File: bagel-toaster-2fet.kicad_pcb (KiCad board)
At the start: 2 copper layers, 144.4 x 105.1 mm, 121 parts, among them J1 bs, J10 9v, J11 9v, J12 9v, J13 9v, J14 o1b, J15 gnd, J16 gnd, J17 gnd, J18 gnd, J19 i2b, J2 do_snd, J20 o2b, J21 i2, J22 i2s, J23 gnd, J24 o2, J25 9v, J26 o2s, J27 i1, J28 i1s, J29 gnd, J3 out, J30 o1, J31 9v, J32 o1s, J4 in, J5 do_rtn, J6 i1b, J7 bs, J8 gnd, J9 9v, Q1 J113, Q2 J201, SW1 3pdt, SW2 Alpha_3PDT, SW3 Alpha_3PDT, SW4 Alpha_3PDT, U1 TL074, U2 4069

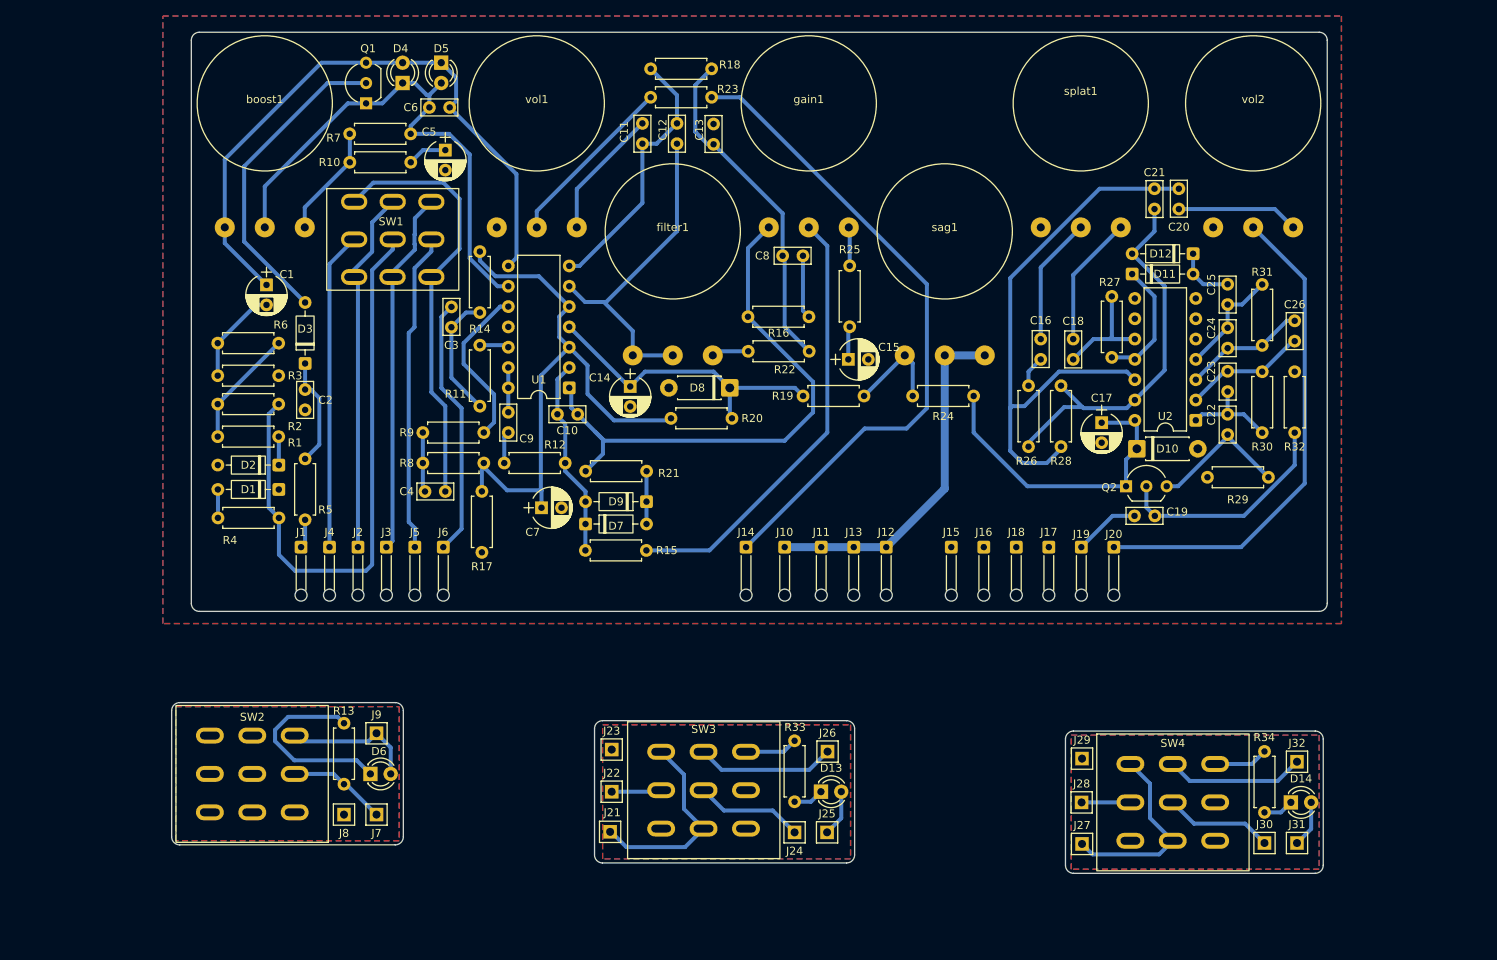
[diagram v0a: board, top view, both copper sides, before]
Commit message: one sided and smaller
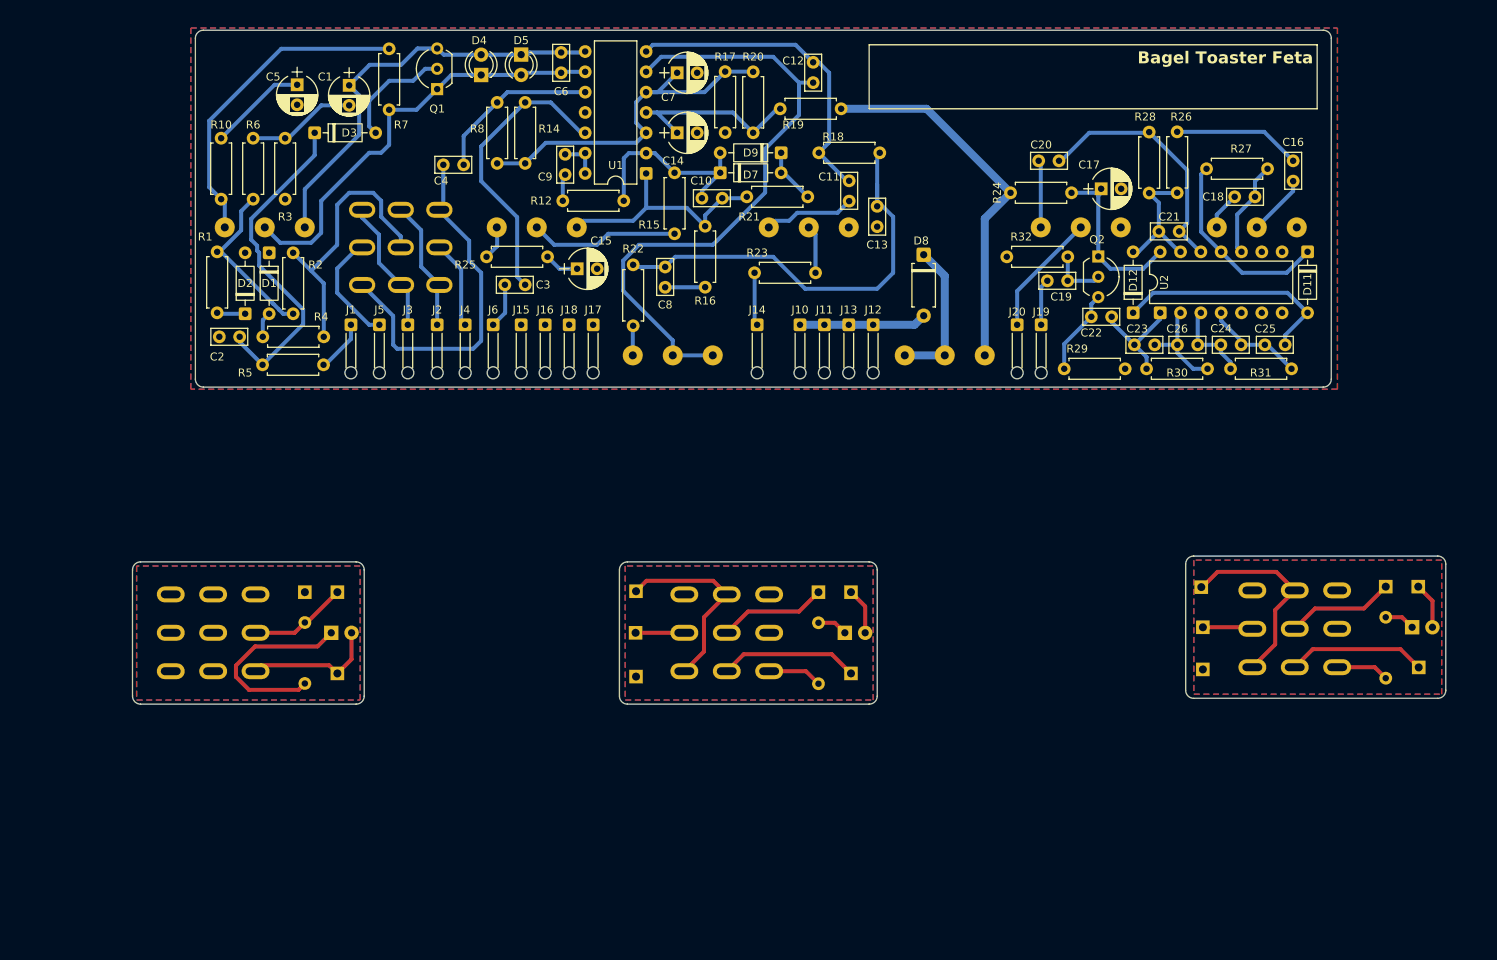
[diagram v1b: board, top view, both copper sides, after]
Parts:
- removed D10: 1N4001, Diode_THT:D_DO-41_SOD81_P7.62mm_Horizontal
- removed R11, R9: 100, 1_trevortjes_lib:R_1x4
- D13, D14, D6, J21, J22, J23, J24, J25, J26, J27, J28, J29, J30, J31, J32, J7, J8, J9, R13, R33, R34, SW1, SW2, SW3, SW4, boost1, filter1, gain1, sag1, splat1, vol1, vol2: moved to B.Cu
- D8: value 1N4001 -> D_Schottky; footprint Diode_THT:D_DO-41_SOD81_P7.62mm_Horizontal -> Diode_THT:D_A-405_P7.62mm_Horizontal
- moved J24 80.0 mm to (214.1, 96.7)
- moved J25 80.0 mm to (218.1, 96.7)
- moved J21 80.0 mm to (191.0, 96.8), turned to 90 degrees
- moved D13 76.7 mm to (217.4, 101.8)
- moved J22 76.7 mm to (191.2, 101.8)
- moved SW3 76.6 mm to (202.7, 102.0)
- moved J26 74.6 mm to (218.2, 106.8)
- moved J23 74.6 mm to (191.2, 107.1)
- moved R33 74.3 mm to (214.1, 108.2), turned to 90 degrees
- moved J27 64.1 mm to (120.4, 97.3)
- moved J30 64.0 mm to (143.2, 97.4)
- moved J31 64.0 mm to (147.2, 97.4)
- moved J17 63.4 mm to (115.0, 64.0)
- moved J18 62.4 mm to (112.0, 64.0)
- moved J16 61.5 mm to (109.0, 64.0)
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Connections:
- C3 pad 2: Net-(C3-Pad2) -> Net-(U1D-+)
- C4 pad 2: Net-(C4-Pad2) -> Net-(U1C-+)
- D8 pad 1: /v2 -> Net-(D8-K)
- D8 pad 2: GND -> /9v
- R14 pad 2: Net-(C3-Pad2) -> Net-(U1D-+)
- R26 pad 1: Net-(C16-Pad2) -> Net-(C16-Pad1)
- R8 pad 1: Net-(C4-Pad2) -> Net-(U1C-+)
- sag1 pad 2: /9v -> Net-(D8-K)
- sag1 pad 3: /9v -> Net-(D8-K)
- splat1 pad 2: Net-(C16-Pad1) -> Net-(C16-Pad2)
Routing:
- net Net-(J14-Pin_1): track 81.9 -> 6.63 mm
- net Net-(J20-Pin_1): track 61.8 -> 15.5 mm
- net Net-(C20-Pad1): track 73.2 -> 31.3 mm
- net /gainOut: track 69.7 -> 29.8 mm
- net /b_rtn: track 74.4 -> 35.1 mm
- net Net-(U1B--): track 42.1 -> 79.2 mm
- net Net-(R15-Pad2): track 55.3 -> 18.7 mm
- net Net-(R19-Pad1): track 12.7 -> 47.2 mm
- net Net-(U1D-+): track 3.66 -> 36.4 mm
- net Net-(D12-A): track 48.1 -> 16.8 mm
- net /d_snd: track 45.4 -> 16.5 mm
- net /fx_out: track 45.5 -> 16.7 mm
- net /9v: track 44.7 -> 15.9 mm
- net /fx_in: track 39.7 -> 11.0 mm
- net /vref: track 74.1 -> 45.7 mm
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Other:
- board size 144.4 x 105.1 mm -> 164.2 x 84.2 mm
- board text added: "Bagel Toaster Feta"

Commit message: tidier
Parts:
- moved J17 50.2 mm to (156.0, 35.0), turned to 180 degrees
- moved J12 30.5 mm to (159.5, 35.0), turned to 180 degrees
- moved C8 18.5 mm to (142.5, 58.0), turned to 180 degrees
- moved C3 13.6 mm to (102.5, 45.5)
- moved C13 12.8 mm to (151.3, 39.0), turned to 0 degrees
- moved R22 9.92 mm to (127.5, 63.0), turned to 180 degrees
- moved C20 8.38 mm to (181.2, 41.0)
- moved D8 8.21 mm to (159.0, 63.0), turned to 90 degrees
- moved R23 5.49 mm to (136.5, 62.8), turned to 90 degrees
- moved C4 4.91 mm to (100.5, 41.5), turned to 90 degrees
- moved J14 4.50 mm to (140.0, 64.0)
- moved C10 4.33 mm to (131.5, 45.0), turned to -90 degrees
- moved J6 3.50 mm to (106.0, 64.0)
- moved R12 3.50 mm to (115.3, 48.5)
- moved R14 3.36 mm to (103.7, 42.0), turned to 0 degrees
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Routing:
- net Net-(U1D-+): track 36.4 -> 11.3 mm
- net /9v: track 15.9 -> 40.1 mm
- net /vref: track 45.7 -> 65.1 mm
- net Net-(J6-Pin_1): track 5.64 -> 20.0 mm
- net Net-(C13-Pad2): track 54.3 -> 42.2 mm
- net Net-(R19-Pad1): track 47.2 -> 59.1 mm
- net Net-(C20-Pad1): track 31.3 -> 20.4 mm
- net Net-(U1B--): track 79.2 -> 68.6 mm
- net Net-(D8-K): track 18.7 -> 9.84 mm
- net /gainOut: track 29.8 -> 35.8 mm
- net Net-(U1C-+): track 21.1 -> 15.2 mm
- net Net-(C20-Pad2): track 8.43 -> 14.0 mm
- net /b_snd: track 45.1 -> 49.6 mm
- net Net-(C8-Pad2): track 5.01 -> 9.37 mm
- net Net-(J14-Pin_1): track 6.63 -> 4.09 mm
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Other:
- board size 164.2 x 84.2 mm -> 164.2 x 83.9 mm

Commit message: smaller
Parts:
- J1: value bs -> bx; footprint Connector_Wire:SolderWire-0.1sqmm_1x01_D0.4mm_OD1mm_Relief -> Connector_Wire:SolderWire-0.5sqmm_1x01_D0.9mm_OD2.1mm
- J10, J11, J12, J13, J14, J15, J16, J17, J18, J19, J2, J20, J3, J4, J5, J6: footprint Connector_Wire:SolderWire-0.1sqmm_1x01_D0.4mm_OD1mm_Relief -> Connector_Wire:SolderWire-0.5sqmm_1x01_D0.9mm_OD2.1mm
- moved J18 47.6 mm to (162.5, 61.2)
- moved J16 46.3 mm to (158.2, 61.2)
- moved J15 45.1 mm to (154.0, 61.2)
- moved J12 34.6 mm to (137.0, 61.2), turned to 0 degrees
- moved J17 28.4 mm to (166.8, 61.2), turned to 0 degrees
- moved R33 26.4 mm to (198.3, 87.0)
- moved D13 26.4 mm to (201.6, 80.7)
- moved J24 26.4 mm to (198.3, 75.6)
- moved J25 26.4 mm to (202.4, 75.6)
- moved J21 26.4 mm to (175.2, 75.7)
- moved J22 26.4 mm to (175.4, 80.7)
- moved J23 26.4 mm to (175.4, 86.0)
- moved J26 26.4 mm to (202.4, 85.7)
- moved SW3 26.4 mm to (186.9, 80.9)
- moved C12 24.2 mm to (118.6, 30.0), turned to 0 degrees
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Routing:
- net Net-(U1B--): track 68.6 -> 16.5 mm
- net Net-(R19-Pad1): track 59.1 -> 12.6 mm
- net Net-(D3-K): track 43.5 -> 9.68 mm
- net Net-(R10-Pad2): track 40.4 -> 9.53 mm
- net Net-(C13-Pad2): track 42.2 -> 12.1 mm
- net Net-(D4-K): track 54.6 -> 25.8 mm
- net Net-(D12-A): track 15.1 -> 40.8 mm
- net Net-(D11-A): track 28.0 -> 5.88 mm
- net /b_snd: track 49.6 -> 28.1 mm
- net /9v: track 40.1 -> 22.9 mm
- net Net-(Q2-G): track 7.04 -> 24.1 mm
- net Net-(D4-A): track 53.0 -> 37.4 mm
- net /gainOut: track 35.8 -> 20.5 mm
- net Net-(C18-Pad1): track 12.3 -> 27.2 mm
- net Net-(R15-Pad2): track 18.7 -> 4.94 mm
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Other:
- board size 164.2 x 83.9 mm -> 141.5 x 62.1 mm
- board text added: "2026-12-27 Shroyer Technology LLC"
- board text added: "Bagel Toaster Feta (Bagel)"
- board text removed: "Bagel Toaster Feta"

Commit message: looking pretty good
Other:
- board size 141.5 x 62.1 mm -> 142.6 x 62.6 mm
- board text added: "20251227 Shroyer Technology LLC"
- board text removed: "2026-12-27 Shroyer Technology LLC"
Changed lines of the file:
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@@
+	)
+	(gr_arc
+		(start 205.025 26.925)
+		(mid 206.439214 27.510786)
+		(end 207.025 28.925)
+		(stroke
+			(width 0.05)
+			(type default)
+		)
+		(layer "Edge.Cuts")
 	)
 	(gr_arc
@@
 	)
 	(gr_line
-		(start 67 27.5)
-		(end 204.5 27.5)
-		(stroke
-			(width 0.05)
-			(type default)
-		)
-		(layer "Edge.Cuts")
-	)
-	(gr_line
 		(start 119.716893 72.7335)
 		(end 119.716893 88.5135)
-		(stroke
-			(width 0.05)
-			(type default)
-		)
-		(layer "Edge.Cuts")
-	)
-	(gr_arc
-		(start 65 29.5)
-		(mid 65.585786 28.085786)
-		(end 67 27.5)
 		(stroke
 			(width 0.05)
@@
 		(layer "Edge.Cuts")
 	)
-	(gr_line
-		(start 206.5 29.5)
-		(end 206.5 62.5)
-		(stroke
-			(width 0.05)
-			(type default)
-		)
-		(layer "Edge.Cuts")
-	)
-	(gr_line
-		(start 65 62.5)
-		(end 65 29.5)
-		(stroke
-			(width 0.05)
-			(type default)
-		)
-		(layer "Edge.Cuts")
-	)
-	(gr_arc
-		(start 206.5 62.5)
-		(mid 205.914214 63.914214)
-		(end 204.5 64.5)
+	(gr_arc
+		(start 66.475 63.85)
+		(mid 65.060786 63.264214)
+		(end 64.475 61.85)
+		(stroke
+			(width 0.05)
+			(type default)
+		)
+		(layer "Edge.Cuts")
+	)
+	(gr_line
+		(start 64.475 61.85)
+		(end 64.475 28.925)
 		(stroke
 			(width 0.05)
@@
 	)
 	(gr_arc
-		(start 67 64.5)
-		(mid 65.585786 63.914214)
-		(end 65 62.5)
-		(stroke
-			(width 0.05)
-			(type default)
-		)
-		(layer "Edge.Cuts")
-	)
-	(gr_arc
 		(start 65.252 72.406)
 		(mid 65.544893 71.698893)
@@
 	)
 	(gr_line
-		(start 204.5 64.5)
-		(end 67 64.5)
+		(start 205.025 63.85)
+		(end 66.475 63.85)
+		(stroke
+			(width 0.05)
+			(type default)
+		)
+		(layer "Edge.Cuts")
+	)
+	(gr_line
+		(start 66.475 26.925)
+		(end 205.025 26.925)
 		(stroke
 			(width 0.05)
@@
 		(start 120.716893 89.5135)
 		(end 150.936 89.5135)
+		(stroke
+			(width 0.05)
+			(type default)
+		)
+		(layer "Edge.Cuts")
+	)
+	(gr_line
+		(start 207.025 28.925)
+		(end 207.025 61.85)
 		(stroke
 			(width 0.05)
@@
 	)
 	(gr_arc
-		(start 204.5 27.5)
-		(mid 205.914214 28.085786)
-		(end 206.5 29.5)
+		(start 64.475 28.925)
+		(mid 65.060786 27.510786)
+		(end 66.475 26.925)
 		(stroke
 			(width 0.05)
@@
 		(layer "Edge.Cuts")
 	)
-	(gr_text "2026-12-27\nShroyer Technology LLC\n"
+	(gr_arc
+		(start 207.025 61.85)
+		(mid 206.439214 63.264214)
+		(end 205.025 63.85)
+		(stroke
+			(width 0.05)
+			(type default)
+		)
+		(layer "Edge.Cuts")
+	)
+	(gr_text "20251227\nShroyer Technology LLC\n"
 		(at 151.5 34.25 0)
 		(layer "F.SilkS")
@@
 		(layer "Cmts.User")
 		(pts
-			(xy 65.5 27.5) (xy 206.5 27.5)
-		)
-		(height -10.6)
+			(xy 173.296 72.778) (xy 205.808 72.778)
+		)
+		(height -3.728)
 		(orientation 0)
 		(format
@@
 			(keep_text_aligned yes)
 		)
-		(gr_text "141"
-			(at 136 15.75 0)
+		(gr_text "32.512"
+			(at 189.552 67.9 0)
 			(layer "Cmts.User")
 			(effects
@@
 		(layer "Cmts.User")
 		(pts
-			(xy 206.5 27.5) (xy 206.5 71.5)
-		)
-		(height 11.86)
+			(xy 205.025 63.85) (xy 205.025 26.925)
+		)
+		(height 7.225)
 		(orientation 1)
 		(format
@@
 			(keep_text_aligned yes)
 		)
-		(gr_text "44"
-			(at 217.21 49.5 90)
+		(gr_text "36.925"
+			(at 211.1 45.3875 90)
 			(layer "Cmts.User")
 			(effects
+				(font
+					(size 1 1)
+					(thickness 0.15)
+				)
+			)
+		)
+	)
+	(dimension
+		(type orthogonal)
+		(layer "Cmts.User")
+		(pts
+			(xy 207.025 28.925) (xy 64.475 28.925)
+		)
+		(height -9.55)
+		(orientation 0)
+		(format
+			(prefix "")
+			(suffix "")
+			(units 3)
+			(units_format 0)
+			(precision 4)
+			(suppress_zeroes yes)
+		)
+		(style
+			(thickness 0.1)
+			(arrow_length 1.27)
+			(text_position_mode 0)
+			(arrow_direction outward)
+			(extension_height 0.58642)
+			(extension_offset 0.5)
+			(keep_text_aligned yes)
+		)
+		(gr_text "142.55"
+			(at 135.75 18.225 0)
+			(layer "Cmts.User")
+			(effects

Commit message: 1590dd
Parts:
- J14: value o1b -> to
- J19: value i2b -> fi
- J20: value o2b -> fo
- J6: value i1b -> bi
- J7: value bs -> bx
- sag1: footprint 1_mylib-footprint:pot-16mm-short-leg -> Potentiometer_THT:Potentiometer_Alpha_RD901F-40-00D_Single_Vertical
- moved SW2 146.3 mm to (216.8, 117.8), turned to -90 degrees
- moved J9 132.1 mm to (221.8, 102.3), turned to 90 degrees
- moved R13 131.6 mm to (215.5, 106.3), turned to 0 degrees
- moved J8 128.7 mm to (211.7, 106.3), turned to -90 degrees
- moved D6 128.7 mm to (216.8, 103.0), turned to 90 degrees
- moved J7 123.8 mm to (211.7, 102.3), turned to -90 degrees
- moved J17 119.8 mm to (74.7, 137.8)
- moved J16 110.4 mm to (78.7, 137.8)
- moved R26 104.6 mm to (152.1, 137.3), turned to 0 degrees
- moved J18 102.7 mm to (94.0, 137.8)
- moved splat1 101.8 mm to (155.9, 129.0), turned to 90 degrees
- moved D11 100.8 mm to (159.8, 131.7), turned to 180 degrees
- moved D12 100.5 mm to (152.1, 134.3), turned to 0 degrees
- moved R27 99.2 mm to (159.8, 128.7), turned to 180 degrees
- moved C18 95.6 mm to (149.6, 128.6)
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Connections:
- net /sg1 renamed Net-(J29-Pin_1)
- net /sg2 renamed Net-(J23-Pin_1)
- net /sg3 renamed Net-(J8-Pin_1)
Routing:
- net /b_snd: track 28.1 -> 58.0 mm
- net Net-(J20-Pin_1): track 9.72 -> 36.8 mm
- net Net-(R19-Pad1): track 12.6 -> 37.9 mm
- net /b_rtn: track 37.3 -> 17.4 mm
- net Net-(J1-Pin_1): track 4.02 -> 19.5 mm
- net /v1: track 27.7 -> 41.3 mm
- net Net-(J19-Pin_1): track 6.72 -> 19.4 mm
- net Net-(C18-Pad1): track 27.2 -> 15.1 mm
- net /vref: track 57.5 -> 47.9 mm
- net Net-(C16-Pad1): track 13.9 -> 4.44 mm
- net Net-(D11-A): track 5.88 -> 13.8 mm
- net Net-(Q2-S): track 8.57 -> 16.5 mm
- net Net-(C24-Pad2): track 19.7 -> 12.2 mm
- net Net-(R1-Pad1): track 19.3 -> 26.7 mm
- net Net-(J6-Pin_1): track 13.3 -> 19.5 mm
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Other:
- board size 142.6 x 62.6 mm -> 174 x 42.9 mm
- board text added: "2025.12.27 Shroyer Technology LLC"
- board text removed: "20251227 Shroyer Technology LLC"

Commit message: remove old images
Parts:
- moved J7 147.5 mm to (64.5, 91.7)
- moved J8 147.5 mm to (64.5, 95.7)
- moved D6 147.5 mm to (69.6, 92.4)
- moved J9 147.5 mm to (74.7, 91.7)
- moved R13 147.5 mm to (68.3, 95.7)
- moved SW2 147.5 mm to (69.6, 107.2)
- moved D12 71.1 mm to (160.6, 63.7)
- moved D4 71.1 mm to (89.5, 32.7)
- moved J14 71.1 mm to (127.5, 67.2)
- moved J3 71.1 mm to (71.3, 67.2)
- moved J4 71.1 mm to (62.9, 67.2)
- moved J5 71.1 mm to (75.7, 67.2)
- moved Q1 71.1 mm to (80.5, 36.8)
- moved R12 71.1 mm to (110.9, 48.8)
- moved R26 71.1 mm to (160.6, 66.7)
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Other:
- board size 174 x 42.9 mm -> 116.6 x 93.1 mm
- board text added: "1590xx dimensions (between screws)"

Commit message: .
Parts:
- moved J14 16.9 mm to (110.6, 67.2)
- moved C15 16.6 mm to (94.2, 60.4), turned to 180 degrees
- moved R23 13.3 mm to (116.6, 60.6), turned to 0 degrees
- moved D8 13.3 mm to (137.4, 63.2)
- moved J10 7.05 mm to (129.6, 67.0)
- moved J11 7.05 mm to (117.6, 67.0)
- moved J12 7.05 mm to (121.6, 67.0)
- moved J13 7.05 mm to (125.6, 67.0)
- moved R25 3.56 mm to (98.8, 55.6), turned to 180 degrees
- moved R15 3.51 mm to (111.0, 55.6)
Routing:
- net Net-(D8-K): track 15.5 -> 5.62 mm
- net Net-(R23-Pad2): track 9.79 -> 16.7 mm
- net Net-(J14-Pin_1): track 3.83 -> 9.09 mm
- net /v2: track 29.1 -> 34.0 mm
- net Net-(R25-Pad1): track 7.95 -> 3.54 mm
- net /9v: track 19.4 -> 15.9 mm
- net Net-(C15-Pad1): track 3.74 -> 6.04 mm
- net /b_snd: track 58.0 -> 59.9 mm
- net Net-(R15-Pad2): track 4.94 -> 3.39 mm
- net Net-(D7-K): track 34.7 -> 35.6 mm
- net /vref: track 47.9 -> 48.7 mm
- net Net-(J1-Pin_1): track 19.5 -> 20.2 mm
